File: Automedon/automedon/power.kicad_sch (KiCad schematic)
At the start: 20 parts, among them J29 3211771, J30 3211771, J31 3211771, J32 3211771, J33 3211771, J34 3211771, J35 3211771, J36 3211771, J37 3211771, J38 3211771, J39 3211771, J40 3211771, J41 3211771, J42 3211771, J43 3211771, J44 3211771

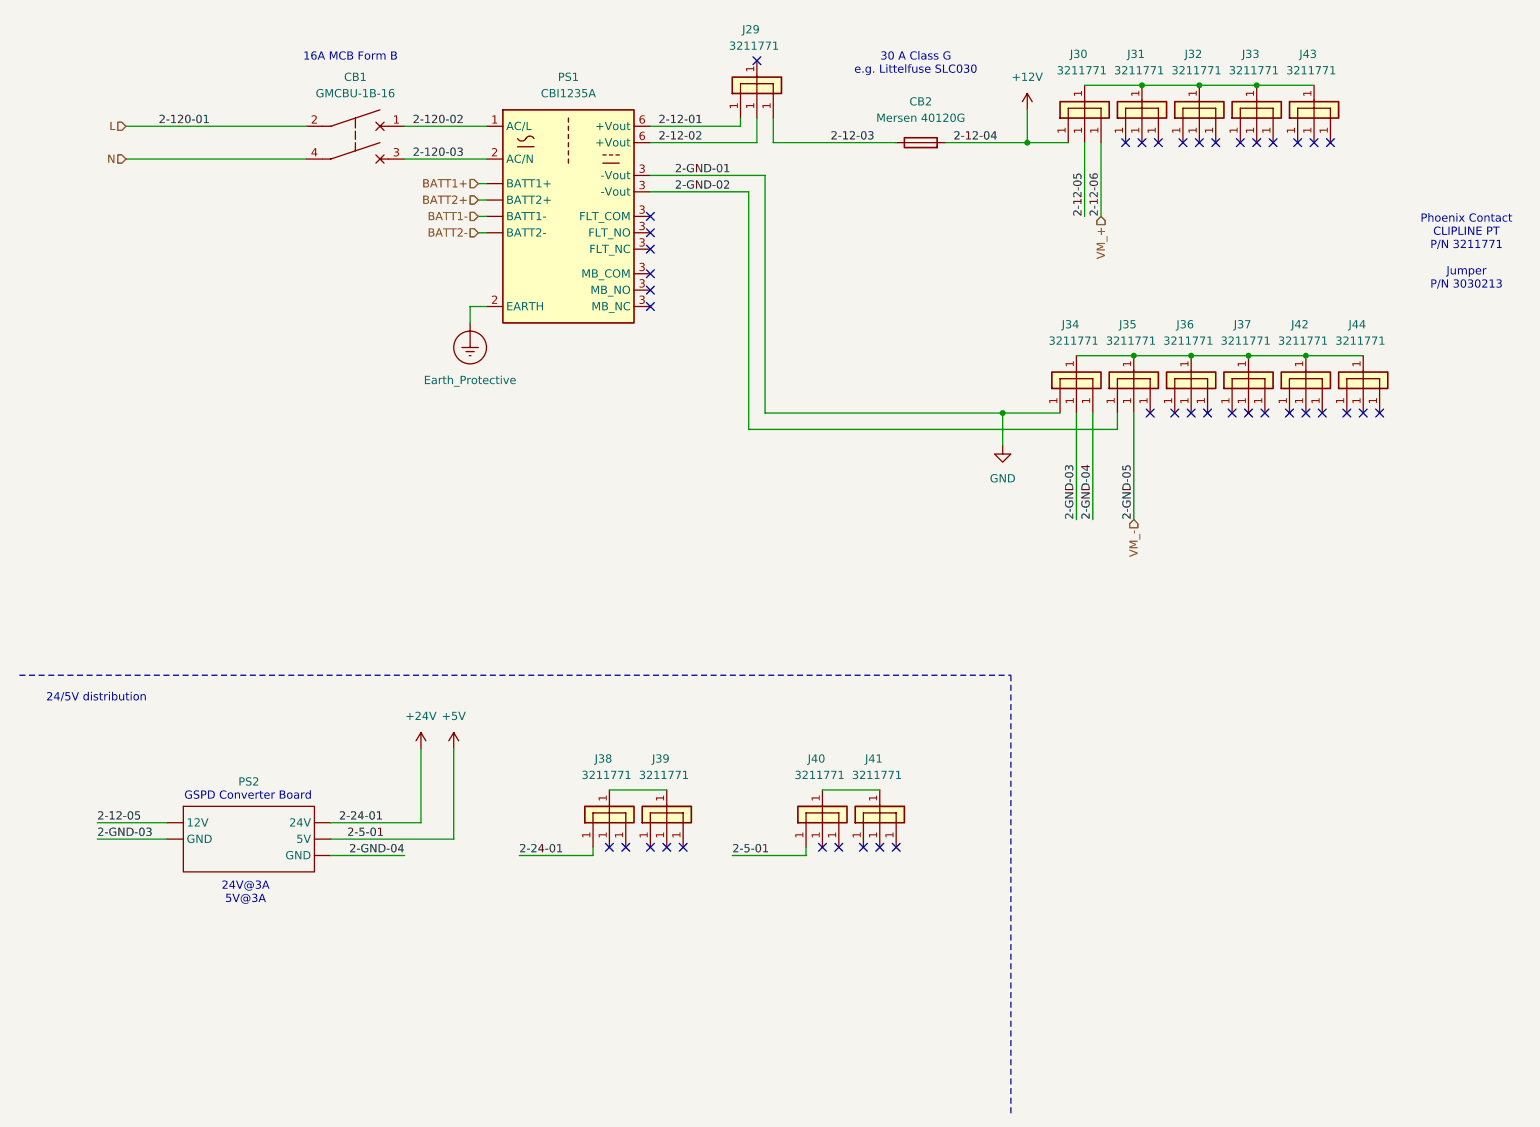
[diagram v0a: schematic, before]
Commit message: Update KiCad schematics and add power converter library
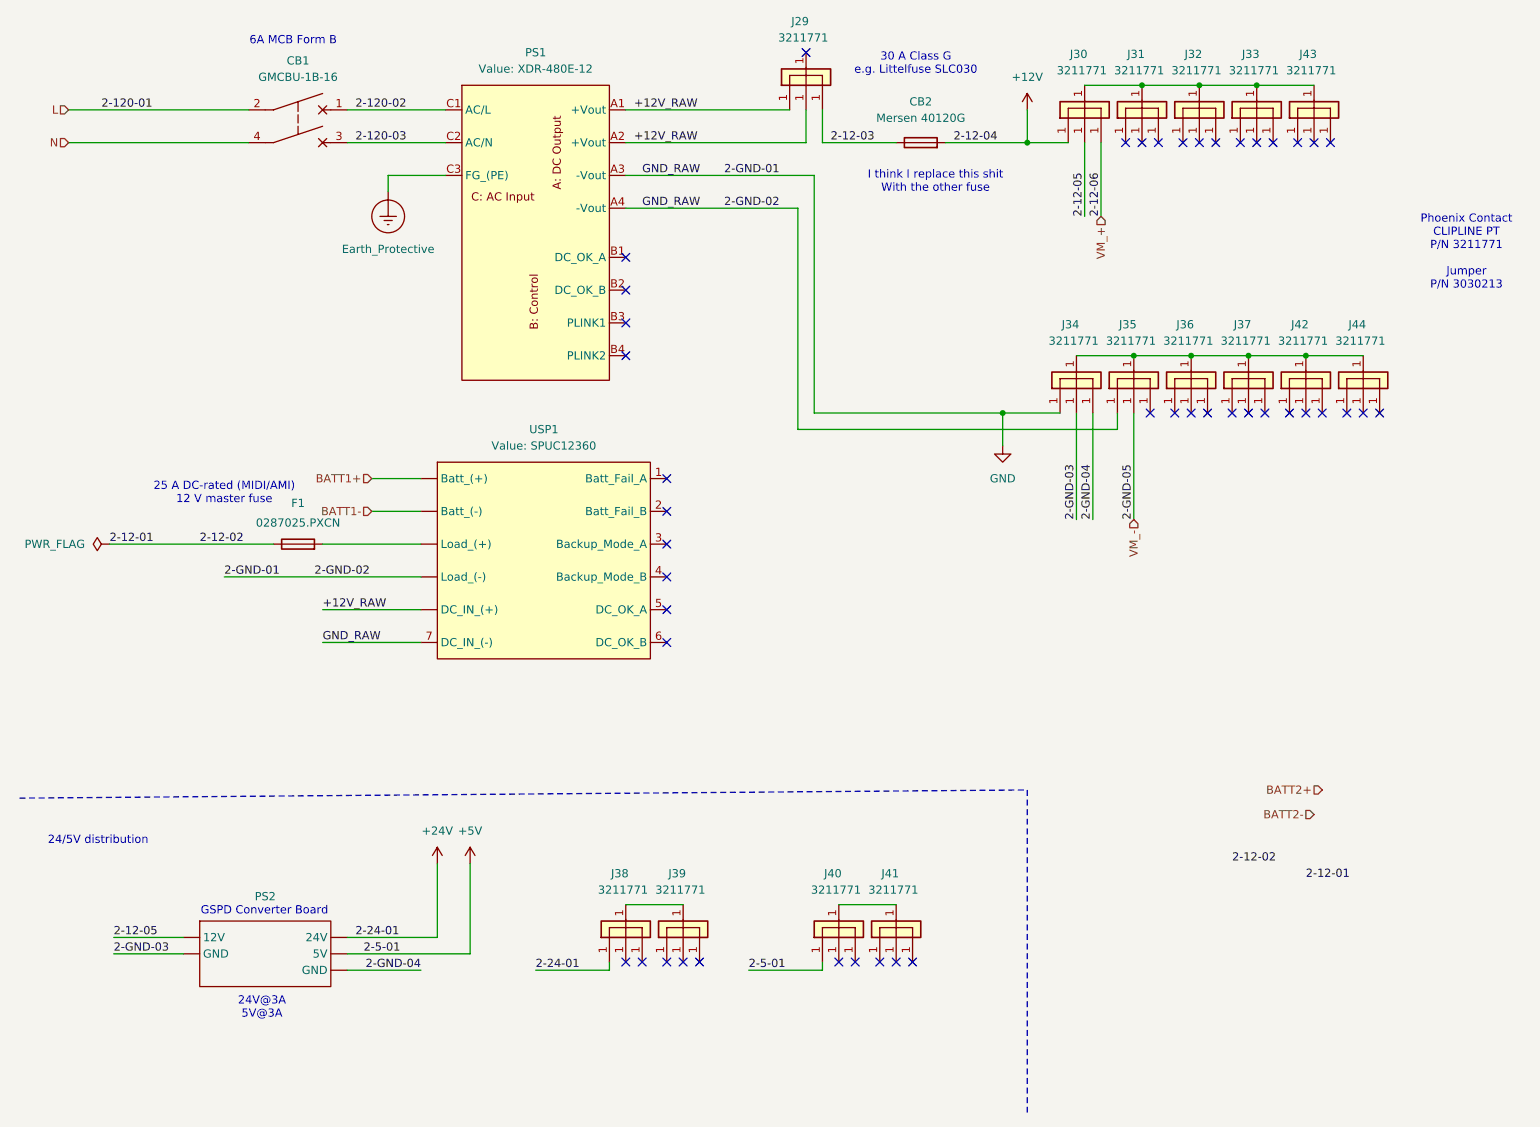
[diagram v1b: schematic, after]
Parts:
- removed PS1: CBI1235A, symbol automedon:CBI12xA
- added F1: 0287025.PXCN, symbol Device:Fuse
- added PS1: XDR-480E-12, symbol UW_Rocketry_Power_Converters:XDR-480E-12
- added USP1: SPUC12360, symbol UW_Rocketry_Power_Converters:SPUC12360
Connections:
- net 2-12-02 is gone; now on net 2-12-03: J29.1
- net 2-GND-02 is gone; now on net VM_-: J35.1
- net 2-12-01: now also F1.1; no longer J29.1 (Pin_3)
- net 2-120-02: now also PS1.C1 (AC/L)
- net 2-120-03: now also PS1.C2 (AC/N)
- net BATT1+: now also USP1. (DC_IN_(+))
- net BATT1-: now also USP1. (DC_IN_(+))
- net Earth_Protective: now also PS1.C3 (FG_(PE))
- net GND: now also J35.1, PS1.A3 (-Vout), PS1.A4 (-Vout), USP1. (DC_IN_(+)), USP1.7 (DC_IN_(-))
- net at J37.1: now also J34.1, J35.1, J36.1, J42.1, J44.1
- net at J39.1: no longer J38.1 (Pin_3)
- net at J41.1: now also J40.1
- new net: J30.1, J31.1, J32.1, J33.1, J43.1
- new net: F1.2, USP1. (DC_IN_(+))
- new net: J38.1, J39.1
- new net +12V_RAW: J29.1, PS1.A1 (+Vout), PS1.A2 (+Vout), USP1. (DC_IN_(+))
- now unconnected: J31.1 (Pin_3), J32.1 (Pin_3), J33.1 (Pin_3), J36.1 (Pin_3), J42.1 (Pin_3), J43.1 (Pin_3), J44.1 (Pin_3)
- no-connect marks 42 -> 46
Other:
- note added: "25 A DC-rated (MIDI/AMI) 12 V master fuse"
- note added: "6A MCB Form B"
- note added: "I think I replace this shit With the other fuse"
- note removed: "16A MCB Form B"
- moved on the sheet: CB1, J29, J38, J39, J40, J41, PS2
